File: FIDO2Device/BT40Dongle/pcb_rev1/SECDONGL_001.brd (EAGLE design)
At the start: 20.4 x 30 mm, 37 parts, among them CN1 CX60-24S-UNIT, CN2 IF_5PIN_H, CN3 IF_2PIN_SOL, SW1 SKRPACE010, SW2 SKTADAE010, U1 BT40, U2 ADP122ACPZ-3.3-R7, U3 RV-3028-C7

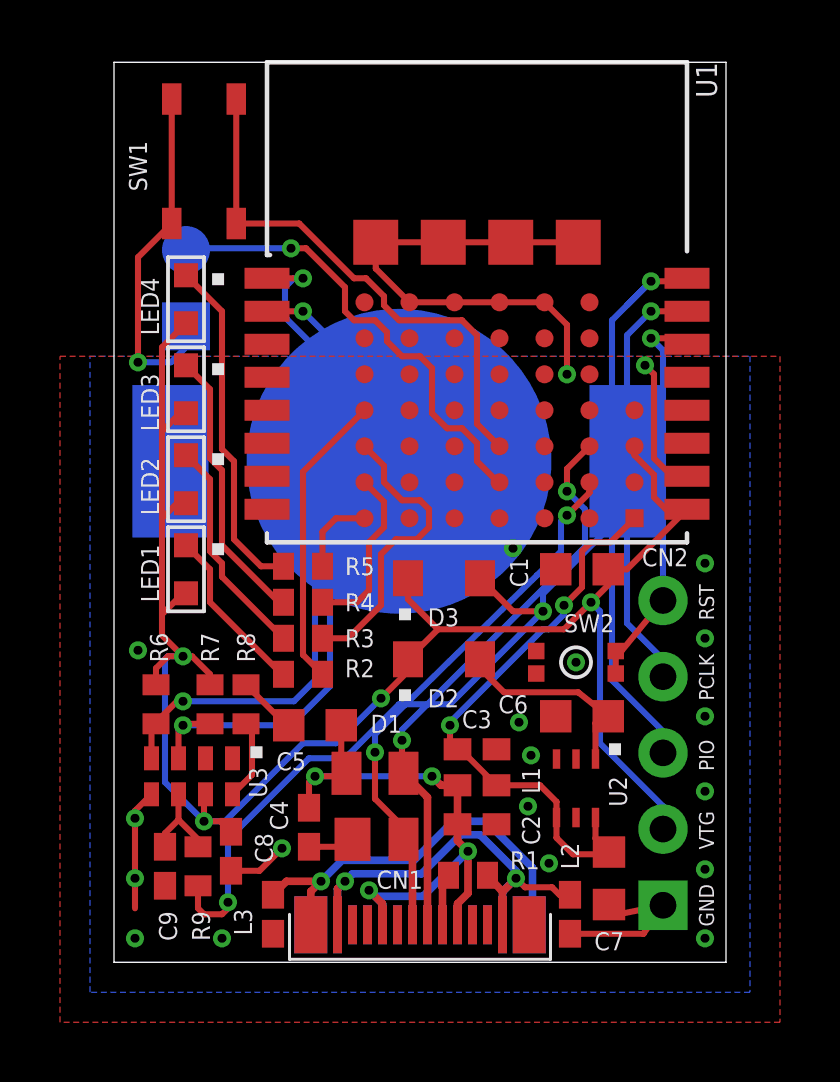
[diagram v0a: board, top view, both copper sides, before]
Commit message: 配線レイアウトを修正
・I2C、LED周りの配線を改善
・一部の周辺部品の位置を移動
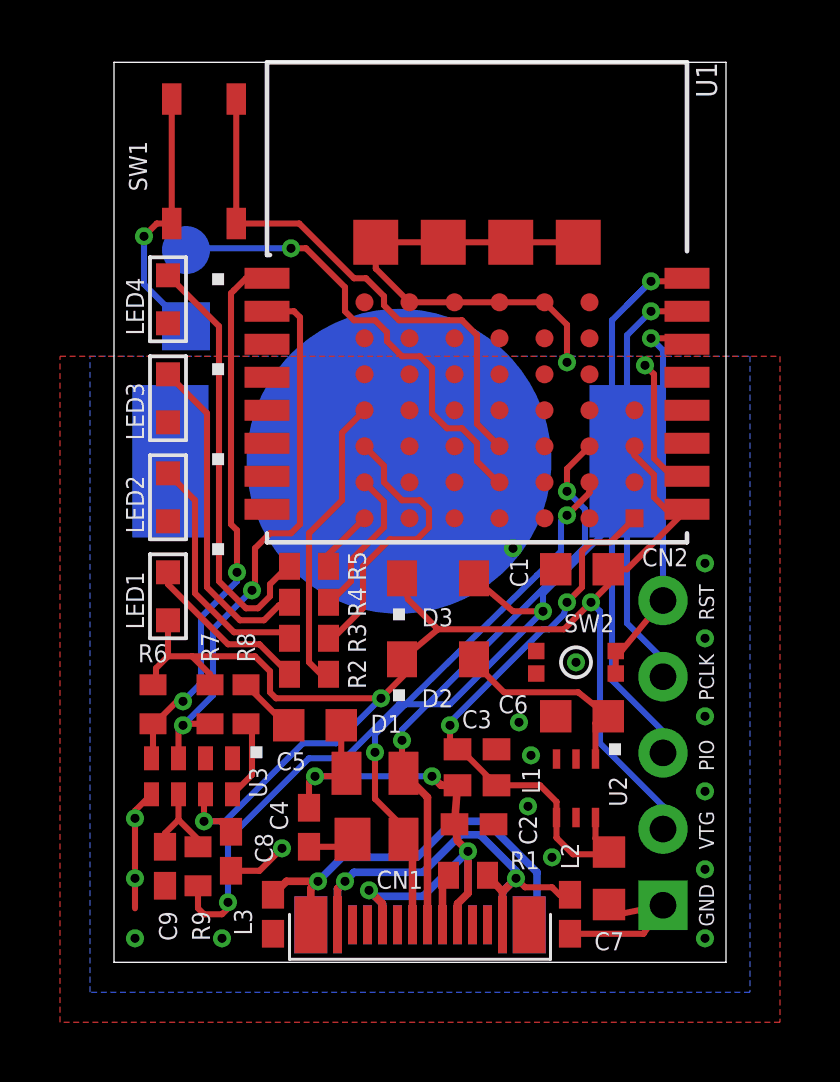
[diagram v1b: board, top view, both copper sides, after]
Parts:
- moved LED1 1.08 mm to (1.80, 12.2)
- moved LED2 0.85 mm to (1.80, 15.5)
- moved LED3 0.67 mm to (1.80, 18.8)
- moved LED4 0.60 mm to (1.80, 22.1)
- moved R2 0.20 mm to (6.50, 9.60)
- moved R3 0.20 mm to (6.50, 10.8)
- moved R4 0.20 mm to (6.50, 12.0)
- moved R5 0.20 mm to (6.50, 13.2)
- moved D2 0.20 mm to (10.8, 10.1)
- moved D3 0.20 mm to (10.8, 12.8)
- moved R6 0.10 mm to (1.30, 8.60)
- moved C2 0.10 mm to (12.0, 4.60)
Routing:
- net VDD_NRF: track 61.4 -> 48.7 mm, vias 4 -> 3
- net SDA: track 22.6 -> 18.3 mm
- net 0V: track 47.9 -> 44.6 mm, vias 21 -> 20
- net N$1: track 11.5 -> 14.4 mm
- net SCL: track 21.6 -> 18.9 mm
- net N$6: track 9.33 -> 11.1 mm
- net LED3: track 5.94 -> 5.21 mm
- net N$7: track 7.45 -> 8.12 mm
- net LED4: track 2.74 -> 2.10 mm

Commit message: 配線レイアウトを修正
・USBを表面で配線させるよう修正
・SWD／RESETを裏面で配線させるよう修正
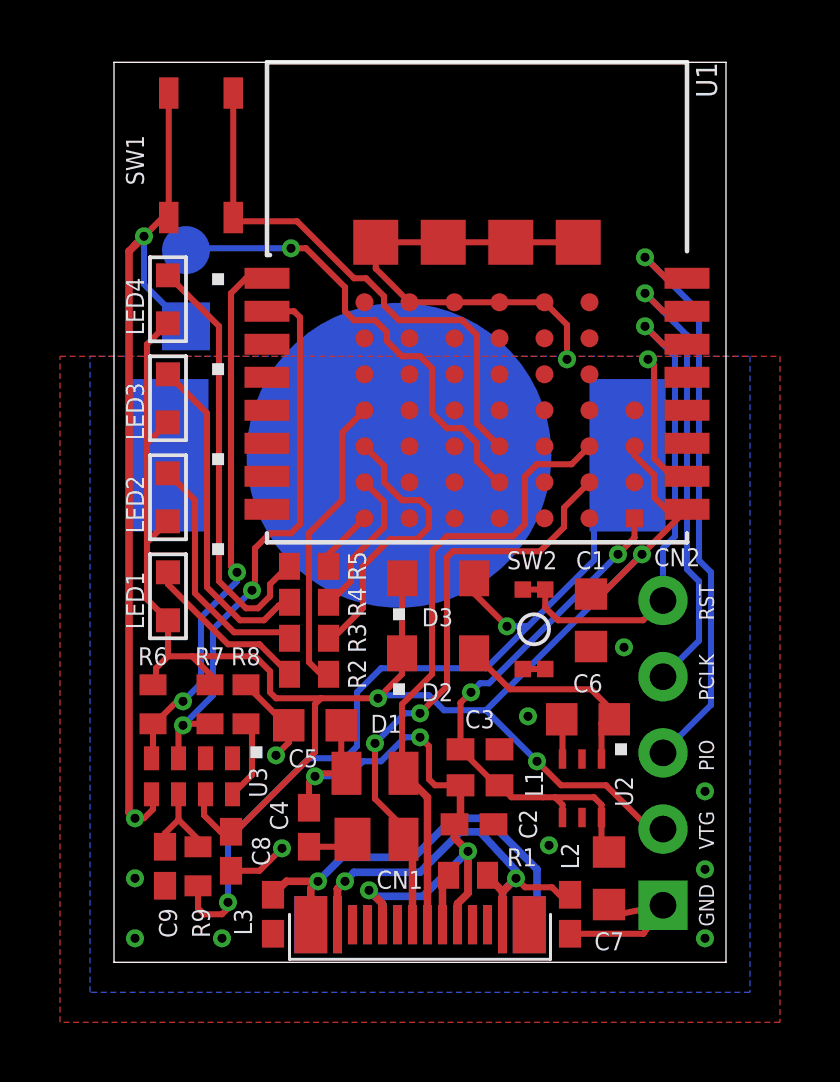
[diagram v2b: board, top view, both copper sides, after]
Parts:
- moved SW2 1.78 mm to (14.0, 11.1), turned to 270 degrees
- moved C1 1.73 mm to (15.9, 11.4), turned to 270 degrees
- moved C6 0.22 mm to (15.8, 8.10)
- moved SW1 0.22 mm to (2.90, 26.9)
- moved D2 0.20 mm to (10.8, 10.3)
- moved BAT1 0.20 mm to (9.50, 16.9)
- moved U2 0.20 mm to (15.6, 5.80)
- moved C3 0.10 mm to (12.2, 7.10)
- moved L1 0.10 mm to (12.2, 5.90)
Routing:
- net 0V: track 44.6 -> 65.2 mm, vias 20 -> 15
- net VDD_NRF: track 48.7 -> 62.3 mm
- net RESET: track 13.3 -> 17.1 mm
- net VBUS: track 22.7 -> 24.8 mm
- net D_N: track 18.3 -> 20.2 mm
- net D_P: track 19.6 -> 21.1 mm, vias 2 -> 0
- net SWCLK: track 14.2 -> 15.7 mm
- net VDD_BAT: track 26.7 -> 28.0 mm
- net VBUS_NRF: track 19.4 -> 18.3 mm

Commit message: 配線レイアウトを修正
・BT40の位置を調整し、裏面べたGNDパターンを改善
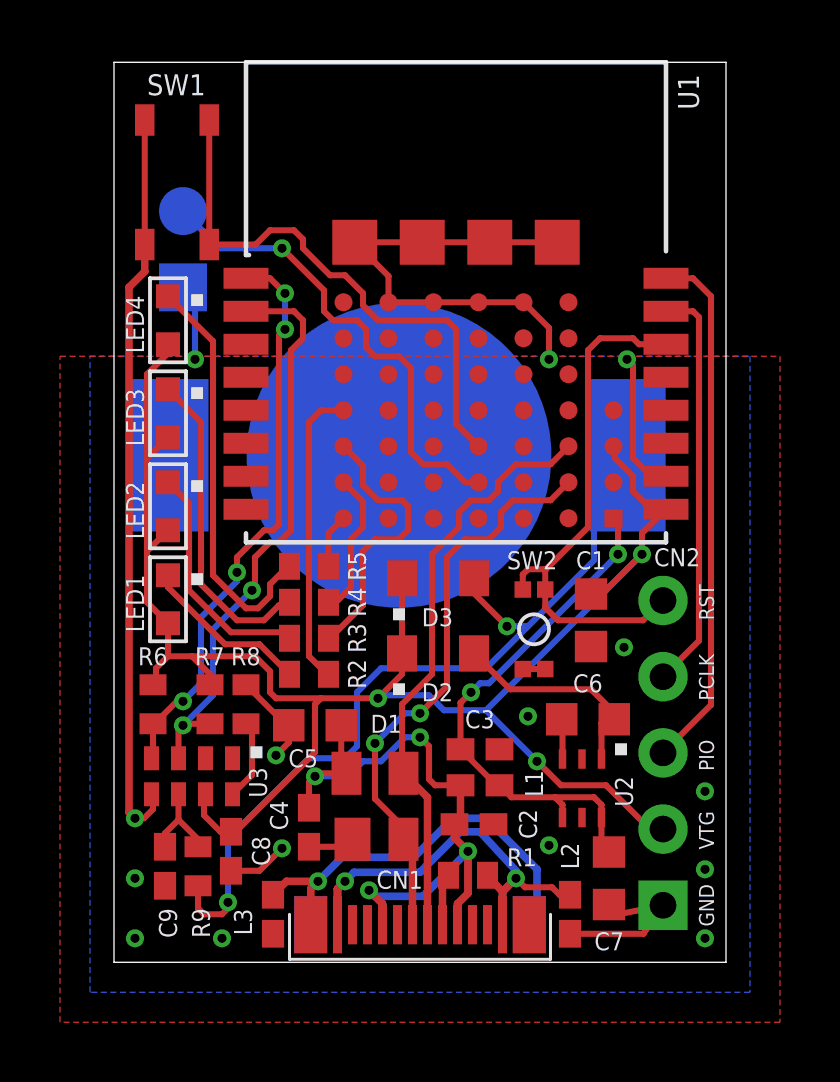
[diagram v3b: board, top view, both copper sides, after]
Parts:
- moved CN3 1.30 mm to (2.30, 22.5)
- moved SW1 1.20 mm to (2.10, 26.0)
- moved LED4 0.70 mm to (1.80, 21.4)
- moved U1 0.70 mm to (4.40, 14.0)
- moved LED3 0.50 mm to (1.80, 18.3)
- moved LED2 0.30 mm to (1.80, 15.2)
- moved LED1 0.10 mm to (1.80, 12.1)
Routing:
- net 0V: track 65.2 -> 62.5 mm
- net SWDIO: track 19.8 -> 17.6 mm, vias 1 -> 0
- net SWCLK: track 15.7 -> 13.7 mm, vias 1 -> 0
- net D_P: track 21.1 -> 19.8 mm
- net VDD_NRF: track 62.3 -> 61.2 mm
- net SDA: track 18.3 -> 19.2 mm, vias 2 -> 4
- net D_N: track 20.2 -> 19.4 mm
- net N$1: track 14.4 -> 13.7 mm
- net RESET: track 17.1 -> 17.7 mm, vias 1 -> 0
- net SCL: track 18.9 -> 19.4 mm

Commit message: 配線レイアウトを修正
・べたGNDパターンを改善
（乾電池ケース周り）
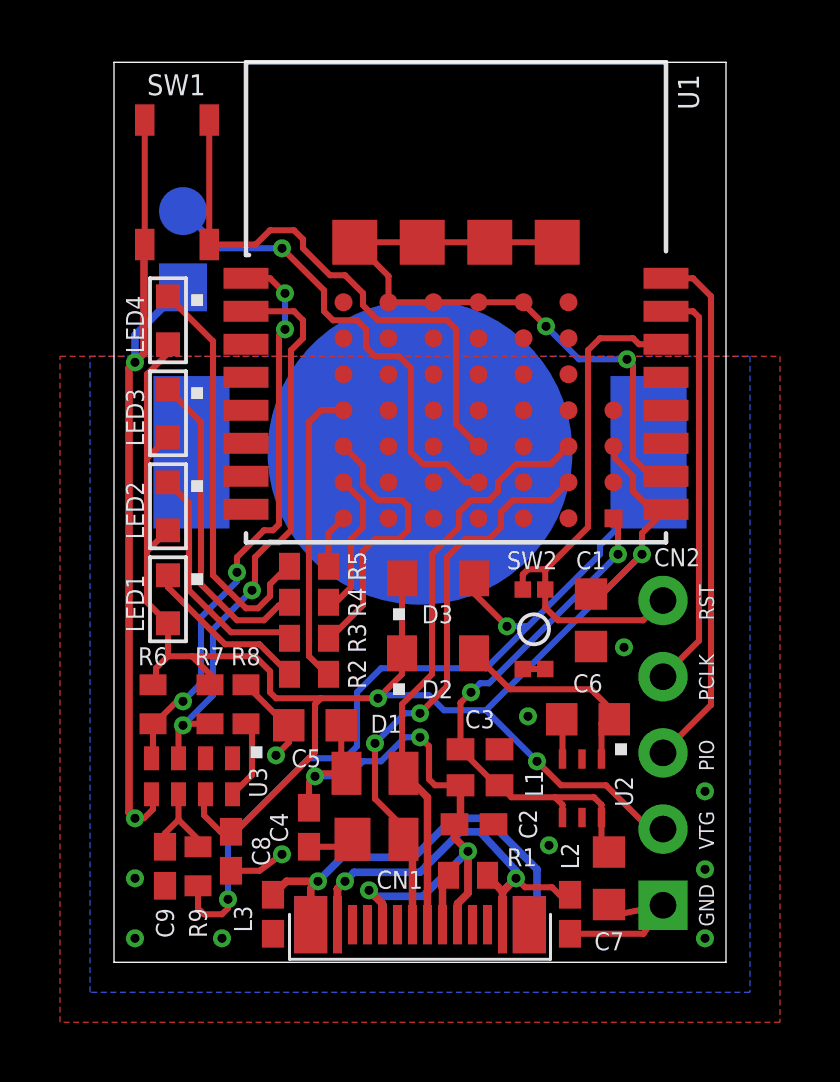
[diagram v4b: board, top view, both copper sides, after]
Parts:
- moved BAT1 0.71 mm to (10.2, 17.0)
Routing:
- net 0V: track 62.5 -> 64.9 mm
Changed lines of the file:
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@@
 </autorouter>
 <elements>
-<element name="BAT1" library="Connectors" package="BAT-HLD-012-SMT" value="BAT-HLD-012-SMT" x="9.5" y="16.9" smashed="yes" rot="MR180">
-<attribute name="NAME" x="8.1" y="23.4" size="0.7" layer="26" rot="MR180"/>
-<attribute name="VALUE" x="19.33" y="16.11" size="0.7" layer="28" rot="MR180"/>
+<element name="BAT1" library="Connectors" package="BAT-HLD-012-SMT" value="BAT-HLD-012-SMT" x="10.2" y="17" smashed="yes" rot="MR180">
+<attribute name="NAME" x="8.8" y="23.5" size="0.7" layer="26" rot="MR180"/>
+<attribute name="VALUE" x="20.03" y="16.21" size="0.7" layer="28" rot="MR180"/>
 </element>
 <element name="C1" library="Parts" package="C0603K" value="4.7uF" x="15.9" y="11.4" smashed="yes" rot="R270">
@@
 </element>
 <element name="C4" library="Parts" package="C0402K" value="0.1uF" x="6.5" y="4.5" smashed="yes" rot="R270">
-<attribute name="NAME" x="5.8" y="4.4" size="0.6" layer="25" rot="R90"/>
+<attribute name="NAME" x="5.8" y="4" size="0.6" layer="25" rot="R90"/>
 <attribute name="VALUE" x="5.129375" y="5.714375" size="0.7112" layer="27" rot="R270"/>
 </element>
 <element name="C5" library="Parts" package="C0603K" value="10uF" x="6.7" y="7.9" smashed="yes" rot="R180">
-<attribute name="NAME" x="6.8" y="7.1" size="0.6" layer="25" rot="R180"/>
+<attribute name="NAME" x="6.9" y="7.1" size="0.6" layer="25" rot="R180"/>
 <attribute name="VALUE" x="7.5" y="9.39125" size="0.7112" layer="27" rot="R180"/>
 </element>
@@
 </element>
 <element name="C9" library="Parts" package="C0402K" value="0.1uF" x="1.7" y="3.2" smashed="yes" rot="R270">
-<attribute name="NAME" x="1.5" y="1.8" size="0.6" layer="25" rot="R270"/>
+<attribute name="NAME" x="1.4" y="1.8" size="0.6" layer="25" rot="R270"/>
 <attribute name="VALUE" x="0.329375" y="4.414375" size="0.7112" layer="27" rot="R270"/>
 </element>
@@
 </element>
 <element name="D2" library="Parts" package="SOD323-W" value="PMEG2005AEA,115" x="10.8" y="10.3" smashed="yes">
-<attribute name="NAME" x="11.3" y="9.3" size="0.6" layer="25" rot="R180"/>
+<attribute name="NAME" x="11.3" y="9.4" size="0.6" layer="25" rot="R180"/>
 <attribute name="VALUE" x="9.63875" y="8.65375" size="0.7112" layer="27" align="top-left"/>
 </element>
 <element name="D3" library="Parts" package="SOD323-W" value="PMEG2005AEA,115" x="10.8" y="12.8" smashed="yes">
-<attribute name="NAME" x="11.3" y="11.8" size="0.6" layer="25" rot="R180"/>
+<attribute name="NAME" x="11.3" y="11.9" size="0.6" layer="25" rot="R180"/>
 <attribute name="VALUE" x="9.63875" y="11.15375" size="0.7112" layer="27" align="top-left"/>
 </element>
@@
 </element>
 <element name="L3" library="Parts" package="C0402K" value="BLM15AG121SN1D" x="5.3" y="1.6" smashed="yes" rot="R270">
-<attribute name="NAME" x="4.6" y="0.9" size="0.6" layer="25" rot="R90"/>
+<attribute name="NAME" x="4.6" y="1" size="0.6" layer="25" rot="R90"/>
 <attribute name="VALUE" x="3.929375" y="2.814375" size="0.7112" layer="27" rot="R270"/>
 </element>
@@
 </element>
 <element name="R9" library="Parts" package="R0402" value="390" x="2.8" y="3.2" smashed="yes" rot="R270">
-<attribute name="NAME" x="2.6" y="1.8" size="0.6" layer="25" rot="R270"/>
+<attribute name="NAME" x="2.5" y="1.8" size="0.6" layer="25" rot="R270"/>
 <attribute name="VALUE" x="1.37125" y="3.755625" size="0.7112" layer="27" rot="R270"/>
 </element>
@@
 </polygon>
 <via x="0.7" y="0.8" extent="1-16" drill="0.3"/>
-<via x="14.5" y="20.1" extent="1-16" drill="0.3"/>
 <wire x1="10.65" y1="22" x2="12.15" y2="22" width="0.2032" layer="1"/>
 <wire x1="12.15" y1="22" x2="13.65" y2="22" width="0.2032" layer="1"/>
@@
 <vertex x="-1.8" y="-2"/>
 </polygon>
-<via x="5.6" y="3.8" extent="1-16" drill="0.3"/>
+<via x="5.6" y="3.6" extent="1-16" drill="0.3"/>
 <wire x1="3.9" y1="3.05" x2="4.85" y2="3.05" width="0.2032" layer="1"/>
-<wire x1="4.85" y1="3.05" x2="5.6" y2="3.8" width="0.2032" layer="1"/>
+<wire x1="4.85" y1="3.05" x2="5.6" y2="3.6" width="0.2032" layer="1"/>
 <wire x1="6.5" y1="3.85" x2="7.7" y2="3.85" width="0.2032" layer="1"/>
 <wire x1="7.7" y1="3.85" x2="7.95" y2="4.1" width="0.2032" layer="1"/>
@@
 <wire x1="14.95" y1="6.775" x2="14.95" y2="8.075" width="0.2032" layer="1"/>
 <wire x1="14.95" y1="8.075" x2="14.925" y2="8.1" width="0.2032" layer="1"/>
-<wire x1="0.5" y1="5" x2="0.7" y2="4.8" width="0.254" layer="1"/>
 <wire x1="1.25" y1="5.6" x2="1.3" y2="5.55" width="0.2032" layer="1"/>
 <wire x1="1.3" y1="5.55" x2="1.3" y2="5.1" width="0.2032" layer="1"/>
 <wire x1="1.3" y1="5.1" x2="1" y2="4.8" width="0.2032" layer="1"/>
 <wire x1="1" y1="4.8" x2="0.7" y2="4.8" width="0.2032" layer="1"/>
-<wire x1="0.5" y1="5" x2="0.5" y2="22.5" width="0.254" layer="1"/>
 <wire x1="13.625" y1="9.775" x2="14.375" y2="9.775" width="0.2032" layer="1"/>
 <wire x1="1.025" y1="28.075" x2="1.025" y2="23.925" width="0.2032" layer="1"/>
@@
 <wire x1="17.3" y1="19.9" x2="17.1" y2="20.1" width="0.2032" layer="1"/>
 <via x="17.1" y="20.1" extent="1-16" drill="0.3"/>
-<wire x1="14.5" y1="20.1" x2="14.5" y2="21.15" width="0.2032" layer="1"/>
-<wire x1="14.5" y1="21.15" x2="13.65" y2="22" width="0.2032" layer="1"/>
 <wire x1="9.15" y1="22" x2="9.15" y2="22.875" width="0.2032" layer="1"/>
 <wire x1="9.15" y1="22.875" x2="8.025" y2="24" width="0.2032" layer="1"/>
 <wire x1="10.65" y1="22" x2="9.15" y2="22" width="0.2032" layer="1"/>
-<via x="2.7" y="20.1" extent="1-16" drill="0.3"/>
-<wire x1="0.5" y1="22.5" x2="1.025" y2="23.025" width="0.254" layer="1"/>
-<wire x1="1.025" y1="23.025" x2="1.025" y2="23.925" width="0.254" layer="1"/>
-<wire x1="2.7" y1="20.1" x2="2.7" y2="22.1" width="0.2032" layer="16"/>
-<wire x1="2.7" y1="22.1" x2="2.3" y2="22.5" width="0.2032" layer="16"/>
+<via x="0.7" y="20" extent="1-16" drill="0.3"/>
+<via x="14.4" y="21.2" extent="1-16" drill="0.3"/>
+<wire x1="17.1" y1="20.1" x2="15.5" y2="20.1" width="0.2032" layer="16"/>
+<wire x1="15.5" y1="20.1" x2="14.4" y2="21.2" width="0.2032" layer="16"/>
+<wire x1="13.65" y1="22" x2="13.65" y2="21.95" width="0.2032" layer="1"/>
+<wire x1="13.65" y1="21.95" x2="14.4" y2="21.2" width="0.2032" layer="1"/>
+<wire x1="0.7" y1="20" x2="0.5" y2="19.8" width="0.254" layer="1"/>
+<wire x1="0.5" y1="19.8" x2="0.5" y2="5" width="0.254" layer="1"/>
+<wire x1="0.5" y1="5" x2="0.7" y2="4.8" width="0.254" layer="1"/>
+<wire x1="0.7" y1="20" x2="1" y2="20.3" width="0.254" layer="1"/>
+<wire x1="1" y1="20.3" x2="1" y2="23.9" width="0.254" layer="1"/>
+<wire x1="1" y1="23.9" x2="1.025" y2="23.925" width="0.254" layer="1"/>
+<wire x1="2.3" y1="22.5" x2="0.7" y2="20.9" width="0.254" layer="16"/>
+<wire x1="0.7" y1="20.9" x2="0.7" y2="20" width="0.254" layer="16"/>
 </signal>
 <signal name="VBUS_NRF">
@@
 <contactref element="D3" pad="A"/>
 <contactref element="R9" pad="2"/>
-<via x="3.8" y="2" extent="1-16" drill="0.3"/>
-<wire x1="3.8" y1="2" x2="3.8" y2="4.1" width="0.2032" layer="16"/>
+<via x="3.8" y="2.1" extent="1-16" drill="0.3"/>
+<wire x1="3.8" y1="2.1" x2="3.8" y2="4.1" width="0.2032" layer="16"/>
 <wire x1="2.8" y1="2.55" x2="2.8" y2="1.8" width="0.2032" layer="1"/>
 <wire x1="2.8" y1="1.8" x2="3" y2="1.6" width="0.2032" layer="1"/>
-<wire x1="3.8" y1="2" x2="3.8" y2="1.8" width="0.2032" layer="1"/>
+<wire x1="3.8" y1="2.1" x2="3.8" y2="1.8" width="0.2032" layer="1"/>
 <wire x1="3.8" y1="1.8" x2="3.6" y2="1.6" width="0.2032" layer="1"/>
 <wire x1="3.6" y1="1.6" x2="3" y2="1.6" width="0.2032" layer="1"/>
 <wire x1="8.9" y1="9.8" x2="12.4" y2="9.8" width="0.2032" layer="16"/>
 <wire x1="12.4" y1="9.8" x2="13.75" y2="11.15" width="0.2032" layer="16"/>
-<wire x1="13.75" y1="11.15" x2="16" y2="13.4" width="0.2032" layer="16"/>
-<wire x1="17.12" y1="16.9" x2="16" y2="15.78" width="0.2032" layer="16"/>
-<wire x1="16" y1="15.78" x2="16" y2="13.4" width="0.2032" layer="16"/>
+<wire x1="13.75" y1="11.15" x2="16.2" y2="13.6" width="0.2032" layer="16"/>
 <wire x1="8.9" y1="9.8" x2="8.1" y2="9" width="0.2032" layer="16"/>
 <wire x1="8.1" y1="9" x2="8.1" y2="7.2" width="0.2032" layer="16"/>
@@
 <wire x1="12" y1="12.8" x2="12" y2="12.3" width="0.2032" layer="1"/>
 <wire x1="12" y1="12.3" x2="13.1" y2="11.2" width="0.2032" layer="1"/>
+<wire x1="16.2" y1="13.6" x2="16.2" y2="13.9" width="0.2032" layer="16"/>
+<wire x1="16.2" y1="13.9" x2="17.6" y2="15.3" width="0.2032" layer="16"/>
+<wire x1="17.6" y1="15.3" x2="17.6" y2="16.78" width="0.2032" layer="16"/>
+<wire x1="17.6" y1="16.78" x2="17.82" y2="17" width="0.2032" layer="16"/>
 </signal>
 <signal name="N$3">
